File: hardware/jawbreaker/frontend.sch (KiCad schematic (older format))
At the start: 114 parts, among them J2 GSG-900MHZ-F-ANTENNA, P4 ANTENNA, Q1 MOSFET_P, Q2 MOSFET_P, T1 MIX_IN_BALUN, T2 MIX_OUT_BALUN, U1 SKY13350, U10 SKY13350, U11 SKY13350, U12 SKY13317, U13 MGA-81563, U14 SKY13317, U15 GSG-74HC04, U16 GSG-74HC08, U2 SKY13350, U25 MGA-81563, U3 RX_LOWPASS_FILTER, U4 RFFC5072, U5 SKY13350, U6 SKY13350, U7 SKY13350, U8 RX_HIGHPASS_FILTER, U9 SKY13317

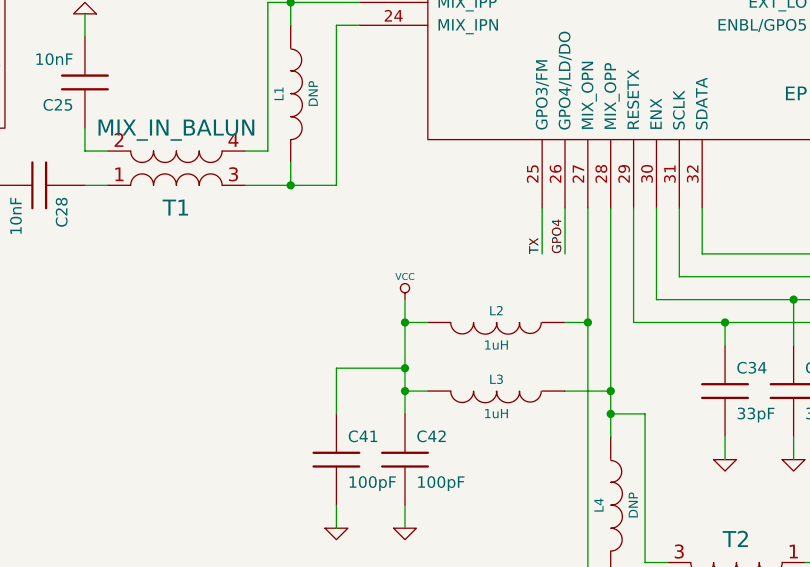
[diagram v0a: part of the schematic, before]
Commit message: moved mixer supply from VCC to VAA
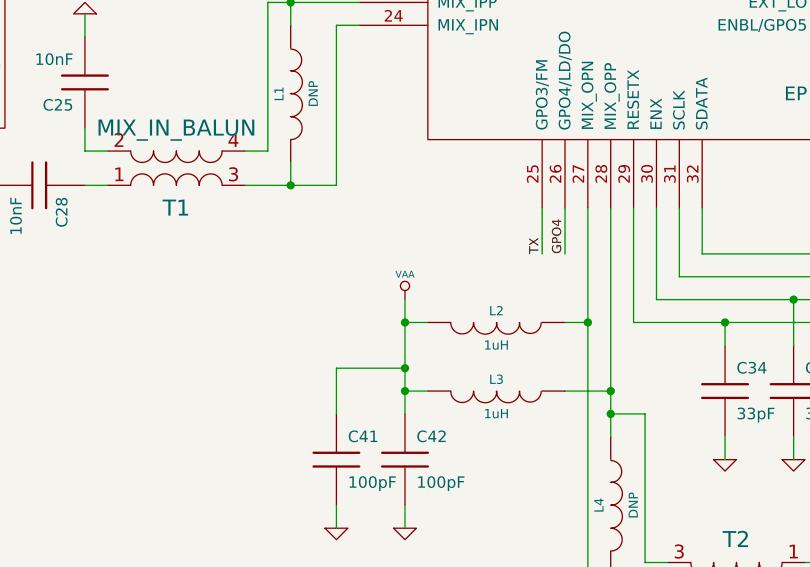
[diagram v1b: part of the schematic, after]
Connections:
- net VAA: now also C41.1, C42.1, L2.2, L3.2
- net VCC: no longer C41.1, C42.1, L2.2, L3.2

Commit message: vertical through-hole SMA connectors
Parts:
- P4: Description CONN FEMALE EDGE MT FOR .062\" BD -> CONN JACK SMA PCB VERT; Manufacturer Linx -> TE Connectivity; Part Number CONSMA003.062 -> 2081233-1
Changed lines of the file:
@@
-EESchema Schematic File Version 2  date Wed Sep  5 11:08:52 2012
+EESchema Schematic File Version 2  date Wed Sep  5 13:31:32 2012
 LIBS:power
 LIBS:device
@@
 F 0 "P4" H 16100 8750 60  0000 C CNN
 F 1 "ANTENNA" H 16100 8450 60  0000 C CNN
-F 4 "Linx" H 16100 8600 60  0001 C CNN "Manufacturer"
-F 5 "CONSMA003.062" H 16100 8600 60  0001 C CNN "Part Number"
-F 6 "CONN FEMALE EDGE MT FOR .062\" BD" H 16100 8600 60  0001 C CNN "Description"
+F 4 "TE Connectivity" H 16100 8600 60  0001 C CNN "Manufacturer"
+F 5 "2081233-1" H 16100 8600 60  0001 C CNN "Part Number"
+F 6 "CONN JACK SMA PCB VERT" H 16100 8600 60  0001 C CNN "Description"
 F 7 "DNP" H 15850 8600 60  0000 C CNN "Note"
 	1    16100 8600

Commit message: shorted resistor symbol, cut trace instead of installing 0402 for antenna mod
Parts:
- removed C164: 10nF, symbol C
- added R44: 0, symbol R-SHORTED
- J2: value GSG-900MHZ-F-ANTENNA -> 900MHZ-F-ANTENNA
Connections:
- net at D1.2 (K), P4.1 (RF): now also C64.2, R44.2
- net at J2.1 (RF): now also R44.1; no longer C64.2
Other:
- note added: "Install P4 and cut R44\nto disable 900 MHx\nPCB antenna and\nenable external antenna."
- moved on the sheet: C64, J2

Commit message: more usage of shorted resistor symbol
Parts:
- removed R83: 0, symbol R
- added R83: 0, symbol R-SHORTED
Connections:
- net !RX_AMP_PWR: now also R83.2; no longer U4.26 (GPO4/LD/DO)
- new net GPO4: R83.1, U4.26 (GPO4/LD/DO)
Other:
- note added: "Install P4 and cut R44\nto disable 900 MHz\nPCB antenna and\nenable external antenna."
- note removed: "Install P4 and cut R44\nto disable 900 MHx\nPCB antenna and\nenable external antenna."
